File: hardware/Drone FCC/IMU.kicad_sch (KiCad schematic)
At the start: 6 parts, among them U1 ICM-42688-P

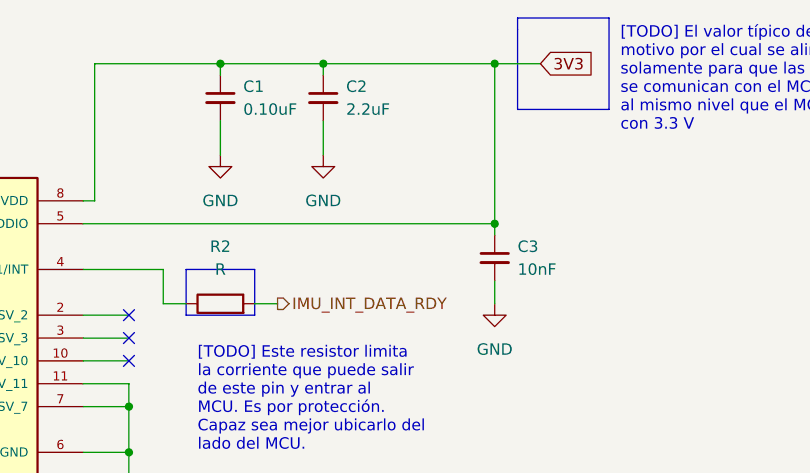
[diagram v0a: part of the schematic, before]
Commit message: esquematico barometro I2C
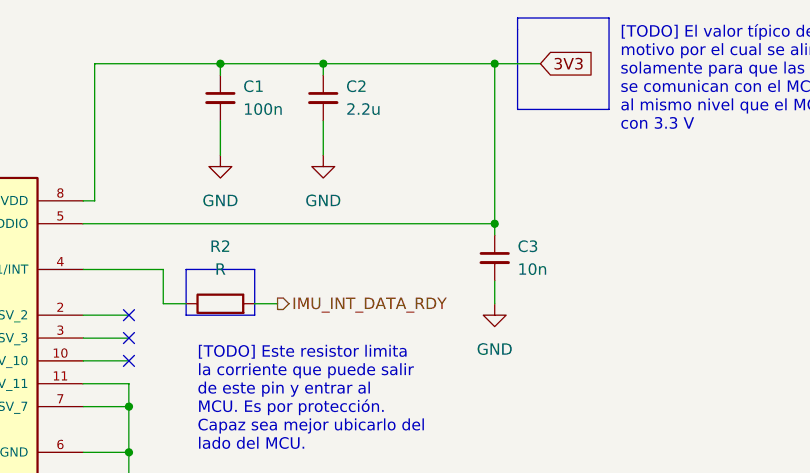
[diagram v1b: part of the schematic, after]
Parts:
- C1: value 0.10uF -> 100n
- C2: value 2.2uF -> 2.2u
- C3: value 10nF -> 10n
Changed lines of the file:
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@@
       (effects (font (size 1.27 1.27)) (justify left))
     )
-    (property "Value" "0.10uF" (id 1) (at 166.37 49.5362 0)
+    (property "Value" "100n" (id 1) (at 166.37 49.5362 0)
       (effects (font (size 1.27 1.27)) (justify left))
     )
@@
       (effects (font (size 1.27 1.27)) (justify left))
     )
-    (property "Value" "10nF" (id 1) (at 196.85 67.3162 0)
+    (property "Value" "10n" (id 1) (at 196.85 67.3162 0)
       (effects (font (size 1.27 1.27)) (justify left))
     )
@@
       (effects (font (size 1.27 1.27)) (justify left))
     )
-    (property "Value" "2.2uF" (id 1) (at 177.8 49.5362 0)
+    (property "Value" "2.2u" (id 1) (at 177.8 49.5362 0)
       (effects (font (size 1.27 1.27)) (justify left))
     )

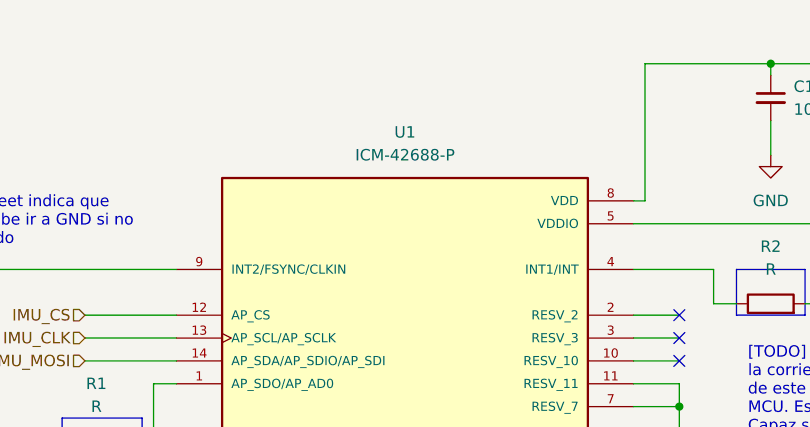
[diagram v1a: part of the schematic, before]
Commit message: changed ICM-42688-P for ICM-42688-V
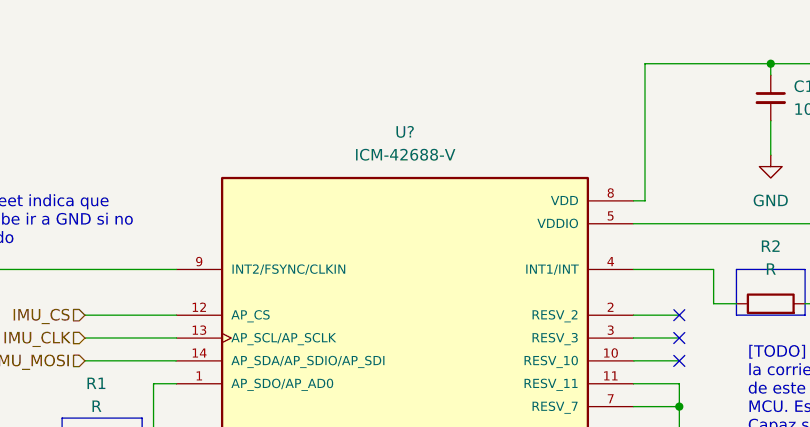
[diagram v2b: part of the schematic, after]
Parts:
- removed U1: ICM-42688-P, PQFN50P300X250X97-14N, symbol ICM-42688-P:ICM-42688-P
- added U?: ICM-42688-V, PQFN50P300X250X97-14N, symbol ICM-42688-V:ICM-42688-V
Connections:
- net 3V3: now also U?.5 (VDDIO), U?.8 (VDD)
- net GND: now also U?.11 (RESV_11), U?.6 (GND), U?.7 (RESV_7), U?.9 (INT2/FSYNC/CLKIN)
- net IMU_CLK: now also U?.13 (AP_SCL/AP_SCLK)
- net IMU_CS: now also U?.12 (AP_CS)
- net IMU_MOSI: now also U?.14 (AP_SDA/AP_SDIO/AP_SDI)
- net at R2.1: now also U?.4 (INT1/INT)
- net at R1.2: now also U?.1 (AP_SDO/AP_AD0)
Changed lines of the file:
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@@
     (pin "2")
+  )
+  (symbol (lib_id "ICM-42688-V:ICM-42688-V") (at 123.19 72.39 0) (unit 1)
+    (in_bom yes) (on_board yes) (fields_autoplaced)
+    (property "Reference" "U?" (id 0) (at 123.19 52.07 0))
+    (property "Value" "ICM-42688-V" (id 1) (at 123.19 54.61 0))
+    (property "Footprint" "PQFN50P300X250X97-14N" (id 2) (at 123.19 72.39 0)
+      (effects (font (size 1.27 1.27)) (justify bottom) hide)
+    )
+    (property "Datasheet" "" (id 3) (at 123.19 72.39 0)
+      (effects (font (size 1.27 1.27)) hide)
+    )
+    (property "MF" "TDK InvenSense" (id 4) (at 123.19 72.39 0)
+      (effects (font (size 1.27 1.27)) (justify bottom) hide)
+    )
+    (property "Description" "Accelerometer, Gyroscope, 6 Axis Sensor Output" (id 5) (at 123.19 72.39 0)
+      (effects (font (size 1.27 1.27)) (justify bottom) hide)
+    )
+    (property "Price" "None" (id 6) (at 123.19 72.39 0)
+      (effects (font (size 1.27 1.27)) (justify bottom) hide)
+    )
+    (property "Purchase-URL" "https://pricing.snapeda.com/search/part/ICM-42688-V/?ref=eda" (id 7) (at 123.19 72.39 0)
+      (effects (font (size 1.27 1.27)) (justify bottom) hide)
+    )
+    (property "Availability" "In Stock" (id 8) (at 123.19 72.39 0)
+      (effects (font (size 1.27 1.27)) (justify bottom) hide)
+    )
+    (property "Package" "Package TDK - InvenSense" (id 9) (at 123.19 72.39 0)
+      (effects (font (size 1.27 1.27)) (justify bottom) hide)
+    )
+    (property "MP" "ICM-42688-V" (id 10) (at 123.19 72.39 0)
+      (effects (font (size 1.27 1.27)) (justify bottom) hide)
+    )
+    (pin "1")
+    (pin "10")
+    (pin "11")
+    (pin "12")
+    (pin "13")
+    (pin "14")
+    (pin "2")
+    (pin "3")
+    (pin "4")
+    (pin "5")
+    (pin "6")
+    (pin "7")
+    (pin "8")
+    (pin "9")
   )
   (symbol (lib_id "power:GND") (at 153.67 91.44 0) (unit 1)
@@
     (pin "1")
   )
-  (symbol (lib_id "ICM-42688-P:ICM-42688-P") (at 123.19 72.39 0) (unit 1)
-    (in_bom yes) (on_board yes) (fields_autoplaced)
-    (property "Reference" "U1" (id 0) (at 123.19 52.07 0))
-    (property "Value" "ICM-42688-P" (id 1) (at 123.19 54.61 0))
-    (property "Footprint" "PQFN50P300X250X97-14N" (id 2) (at 123.19 72.39 0)
-      (effects (font (size 1.27 1.27)) (justify left bottom) hide)
-    )
-    (property "Datasheet" "" (id 3) (at 123.19 72.39 0)
-      (effects (font (size 1.27 1.27)) (justify left bottom) hide)
-    )
-    (property "MANUFACTURER" "TDK InvenSense" (id 4) (at 123.19 72.39 0)
-      (effects (font (size 1.27 1.27)) (justify left bottom) hide)
-    )
-    (property "MAXIMUM_PACKAGE_HEIGHT" "0.97mm" (id 5) (at 123.19 72.39 0)
-      (effects (font (size 1.27 1.27)) (justify left bottom) hide)
-    )
-    (property "STANDARD" "IPC-7351B" (id 6) (at 123.19 72.39 0)
-      (effects (font (size 1.27 1.27)) (justify left bottom) hide)
-    )
-    (property "PARTREV" "1.2" (id 7) (at 123.19 72.39 0)
-      (effects (font (size 1.27 1.27)) (justify left bottom) hide)
-    )
-    (pin "1")
-    (pin "10")
-    (pin "11")
-    (pin "12")
-    (pin "13")
-    (pin "14")
-    (pin "2")
-    (pin "3")
-    (pin "4")
-    (pin "5")
-    (pin "6")
-    (pin "7")
-    (pin "8")
-    (pin "9")
-  )
 )

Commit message: started schematic
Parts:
- U1: renamed from U?; footprint PQFN50P300X250X97-14N -> ICM-42688-V:PQFN50P300X250X97-14N
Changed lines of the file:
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@@
   (symbol (lib_id "ICM-42688-V:ICM-42688-V") (at 123.19 72.39 0) (unit 1)
     (in_bom yes) (on_board yes) (fields_autoplaced)
-    (property "Reference" "U?" (id 0) (at 123.19 52.07 0))
+    (property "Reference" "U1" (id 0) (at 123.19 52.07 0))
     (property "Value" "ICM-42688-V" (id 1) (at 123.19 54.61 0))
-    (property "Footprint" "PQFN50P300X250X97-14N" (id 2) (at 123.19 72.39 0)
+    (property "Footprint" "ICM-42688-V:PQFN50P300X250X97-14N" (id 2) (at 123.19 72.39 0)
       (effects (font (size 1.27 1.27)) (justify bottom) hide)
     )
